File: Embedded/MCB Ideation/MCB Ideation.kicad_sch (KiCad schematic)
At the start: 16 parts, among them J3 MicroSD, U1 Sensored, U4 AP7366-33W5-7

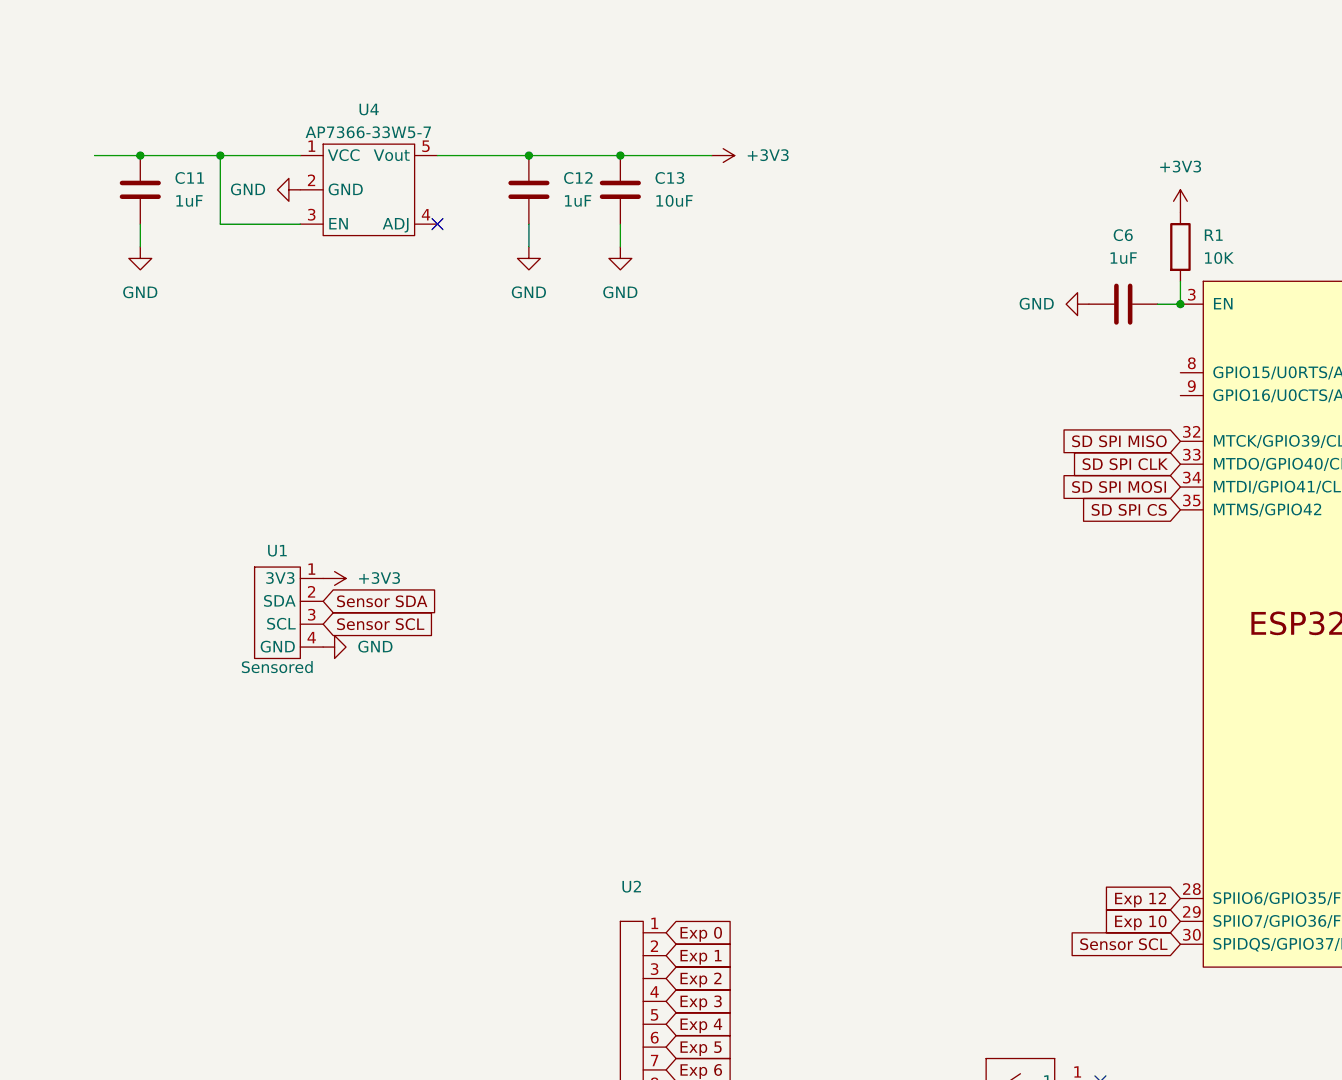
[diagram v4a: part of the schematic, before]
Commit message: Added Secondary Expansion (Comms Link)
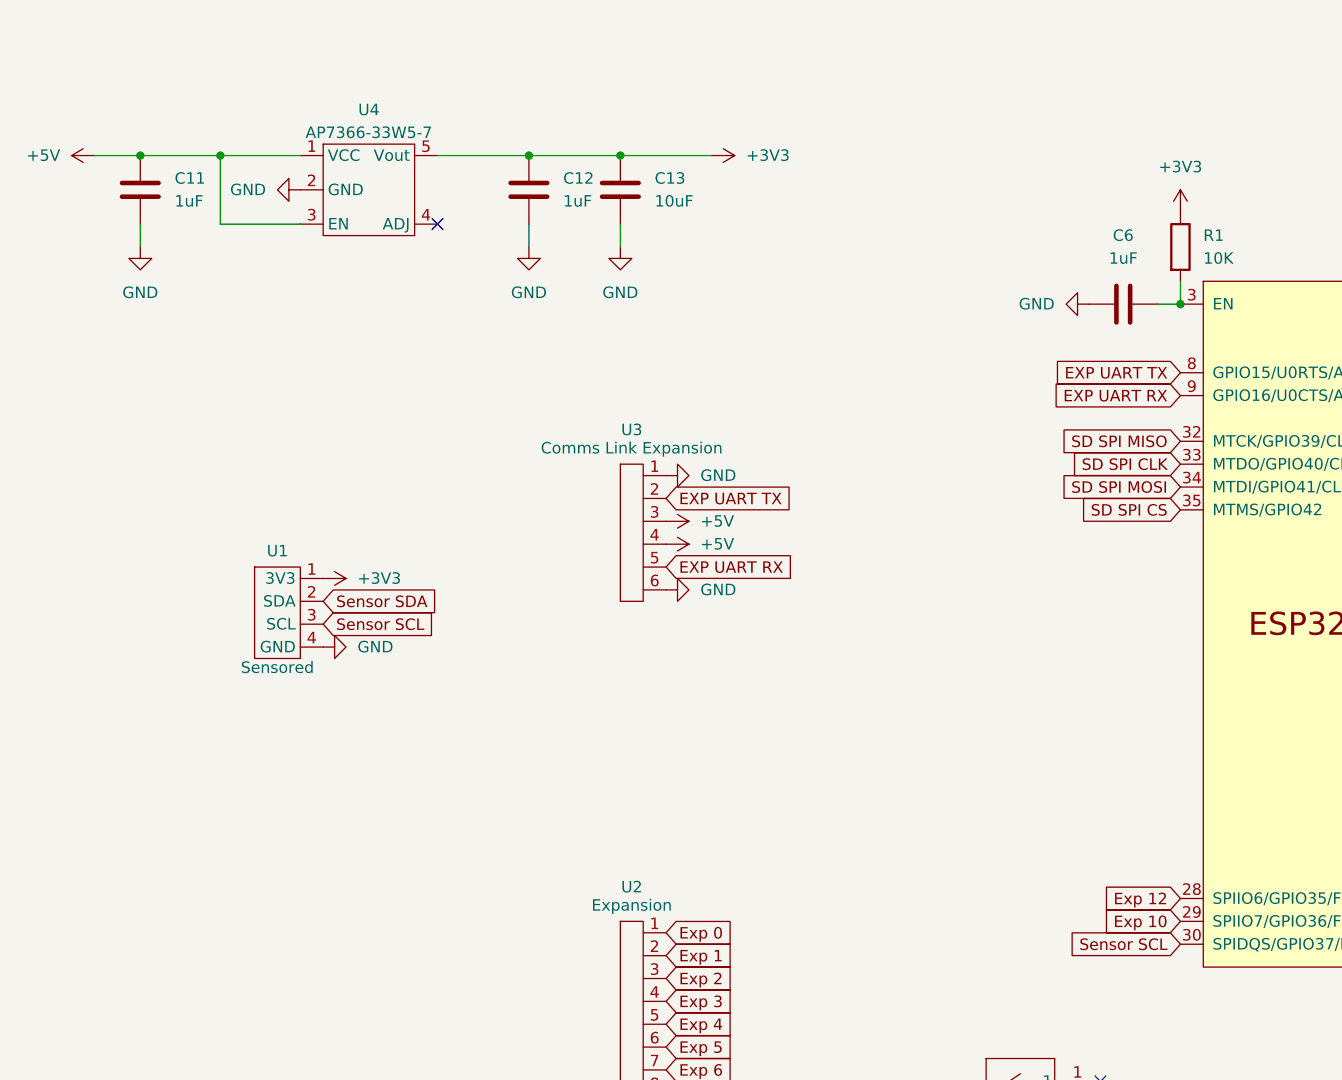
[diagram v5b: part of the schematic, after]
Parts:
- added U3: Comms Link Expansion, FFC_Connector:FFC Aliexpress 0.5mm 6P, symbol FCC_Connector:FFC_6P
- U2: value ~ -> Expansion
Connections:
- net GND: now also U3.1, U3.6
- net EXP UART TX: now reaches ESP1.8 (GPIO15/U0RTS/ADC2_CH4/XTAL_32K_P)
- net EXP UART TX: now also U3.2
- net EXP UART RX: now reaches ESP1.9 (GPIO16/U0CTS/ADC2_CH5/XTAL_32K_N)
- net EXP UART RX: now also U3.5
- net +5V: now reaches C11.1, U4.1 (VCC), U4.3 (EN)
- net +5V: now also U3.3, U3.4

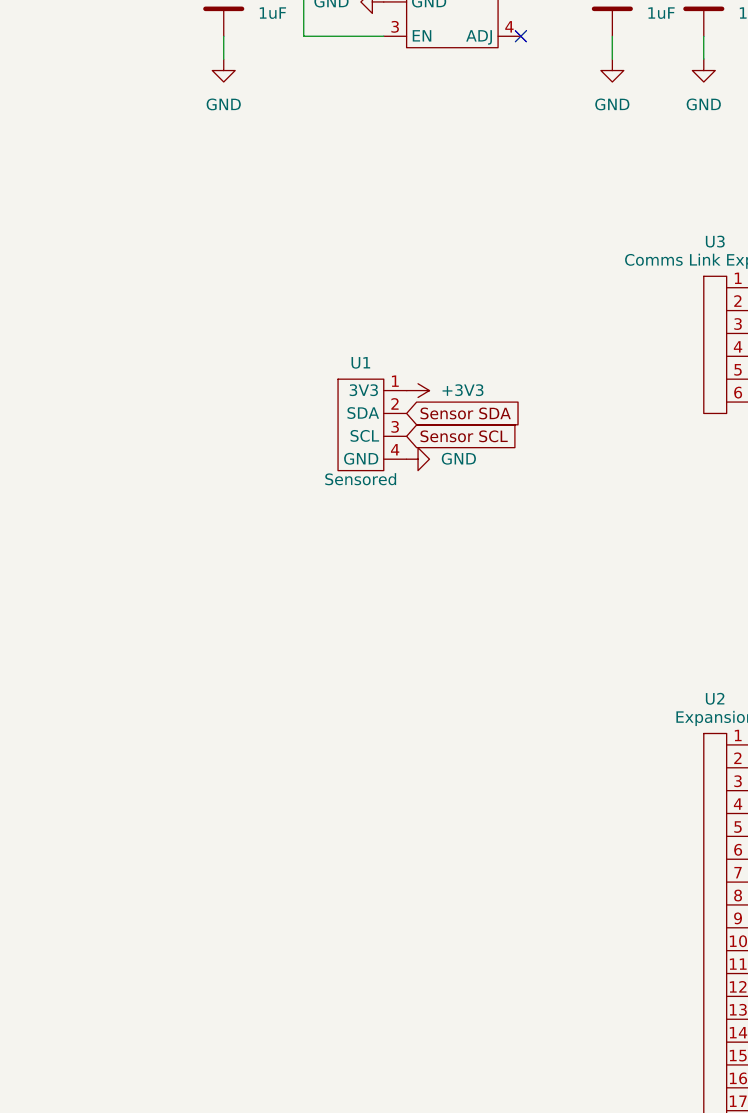
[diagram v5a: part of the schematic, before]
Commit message: Added USB and Power Ports
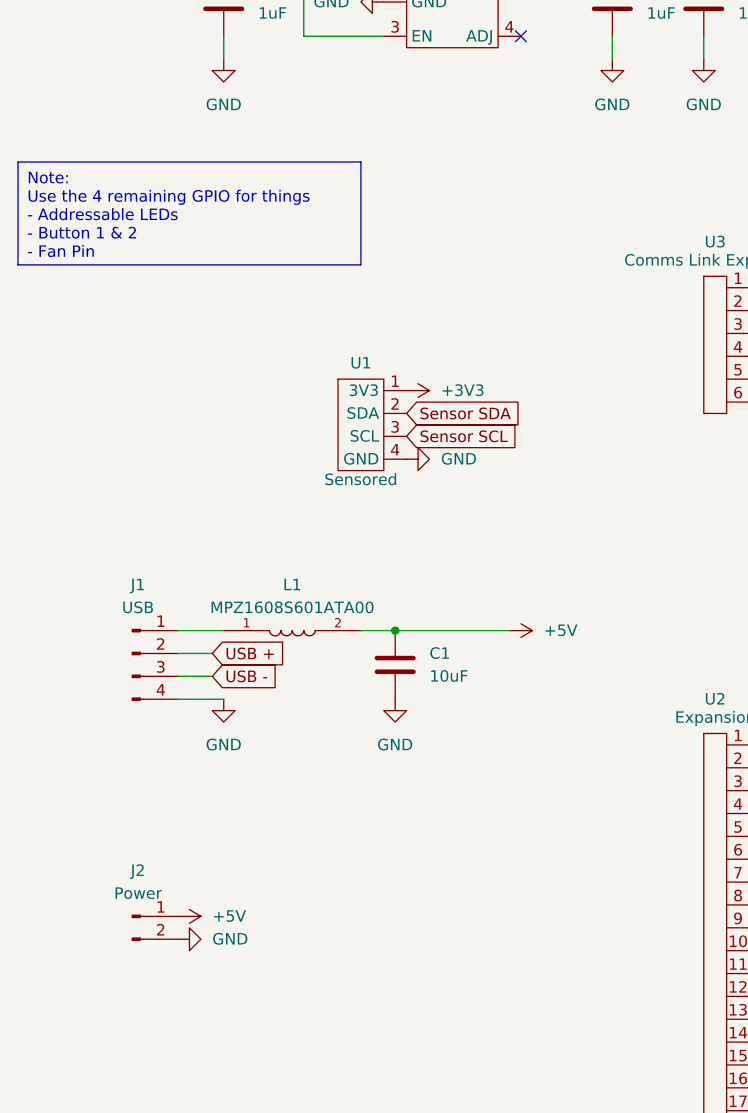
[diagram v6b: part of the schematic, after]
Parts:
- added C1: 10uF, Capacitor_SMD:C_0603_1608Metric, symbol Device:C
- added J1: USB, Connector_Hirose:Hirose_DF13-04P-1.25DS_1x04_P1.25mm_Horizontal, symbol Connector:Conn_01x04_Pin
- added J2: Power, Connector_Hirose:Hirose_DF13-02P-1.25DS_1x02_P1.25mm_Horizontal, symbol Connector:Conn_01x02_Pin
- added L1: MPZ1608S601ATA00, Ferrite_Bead_MPZ1608S601ATA00:INDC1608X95N, symbol Ferrite_Bead_MPZ1608S601ATA00:MPZ1608S601ATA00
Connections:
- net +5V: now also C1.1, J2.1 (Pin_1), L1.2
- net GND: now also C1.2, J1.4 (Pin_4), J2.2 (Pin_2)
- net USB +: now also J1.2 (Pin_2)
- net USB -: now also J1.3 (Pin_3)
- new net: J1.1 (Pin_1), L1.1

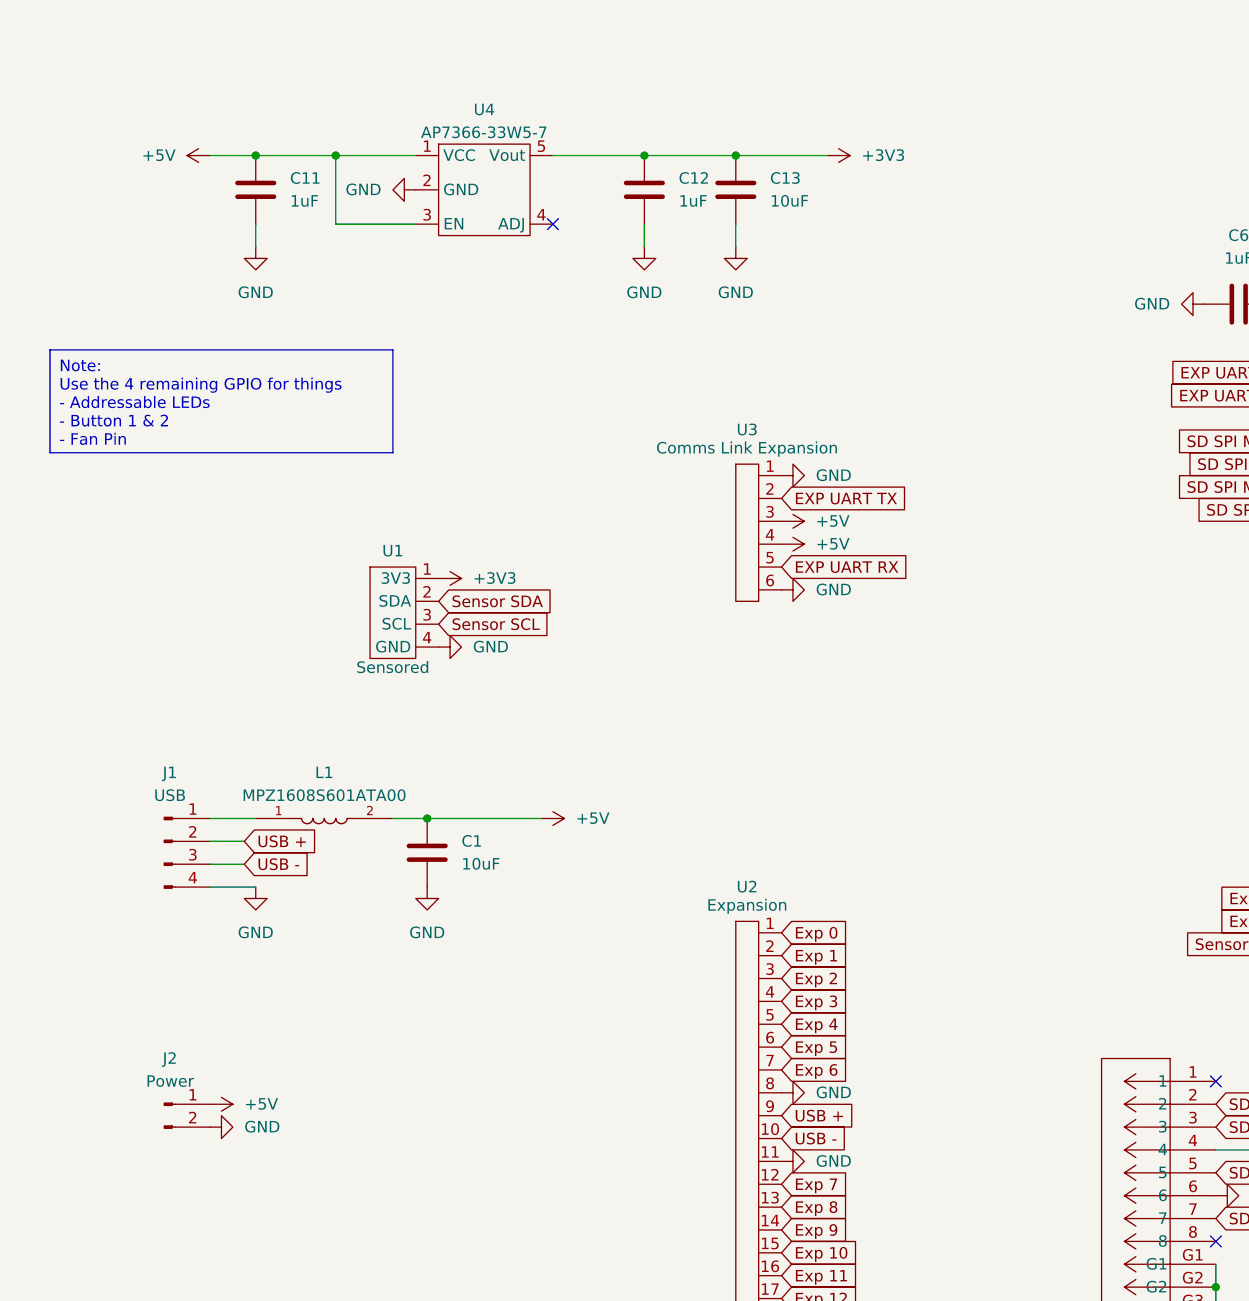
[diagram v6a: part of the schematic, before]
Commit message: Rerouted Some Components
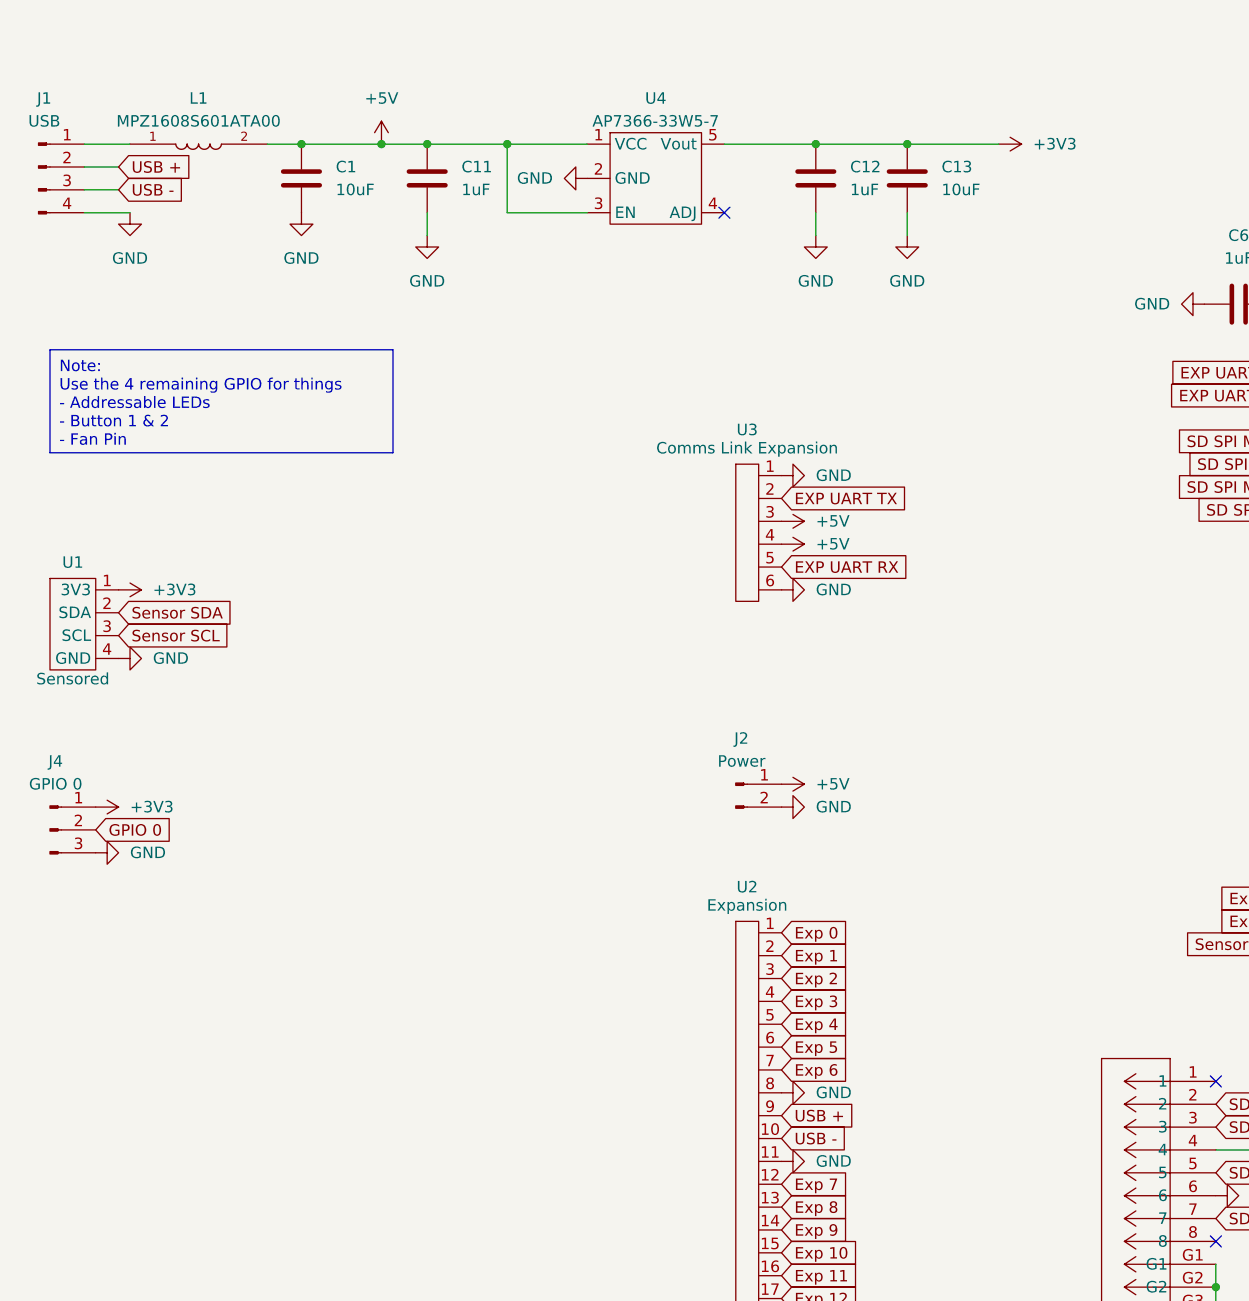
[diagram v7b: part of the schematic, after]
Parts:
- added J4: GPIO 0, symbol Connector:Conn_01x03_Pin
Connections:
- net +3V3: now also J4.1 (Pin_1)
- net GND: now also J4.3 (Pin_3)
- new net GPIO 0: J4.2 (Pin_2)
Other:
- moved on the sheet: C1, C11, C12, C13, J1, J2, L1, U1, U4
